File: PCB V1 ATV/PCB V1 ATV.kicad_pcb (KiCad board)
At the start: 2 copper layers, 101.6 x 53.3 mm, 26 parts, among them J1 Power, J10 NW Sensor, J11 N Sensor, J12 NE Sensor, J13 SW Sensor, J14 S Sensor, J15 SE Sensor, J16 Joystick, J17 MotorControl, J2 PWM, J3 Analog, J4 PWM, J5 Analog, J6 Communication, J7 Digital, J8 Battery 12vIN, J9 Motor Controller, SW1 EStop, U1 L7809

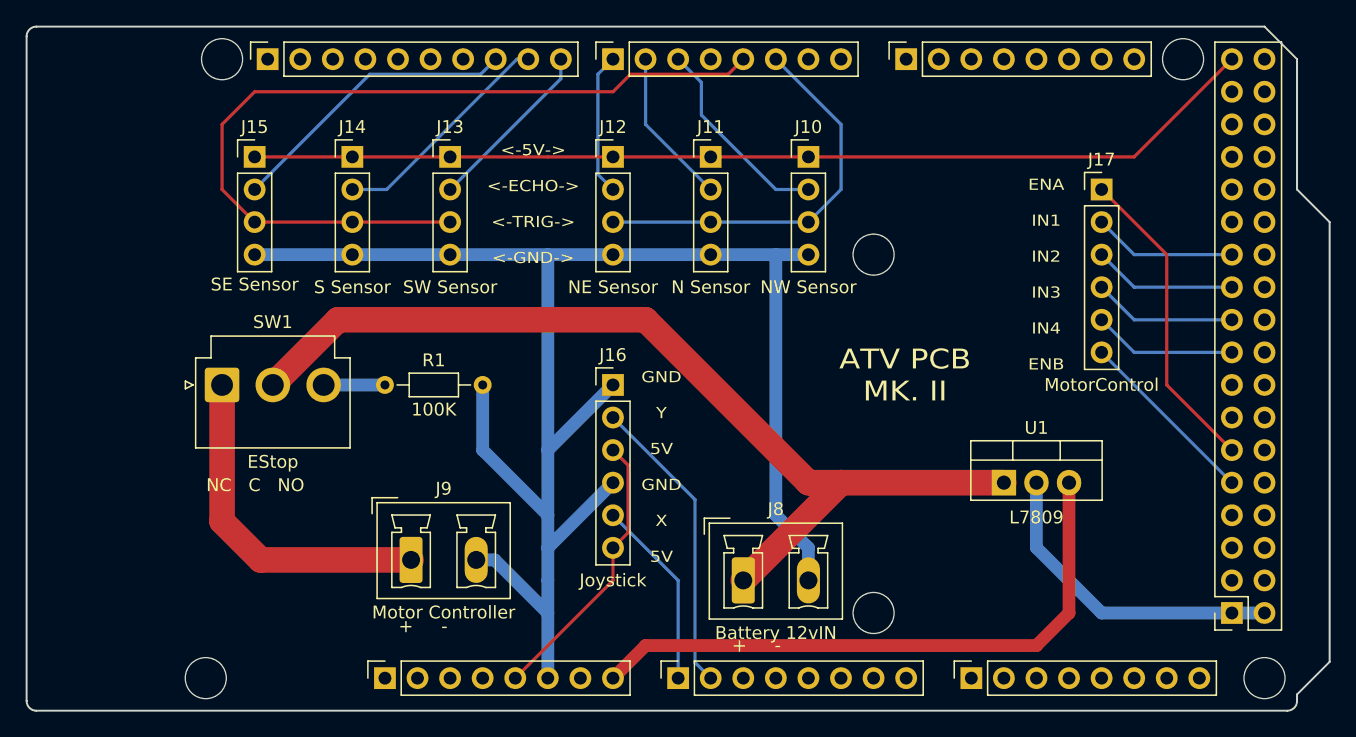
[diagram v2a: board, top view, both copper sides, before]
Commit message: V1.2.1
Updated the silkscreens
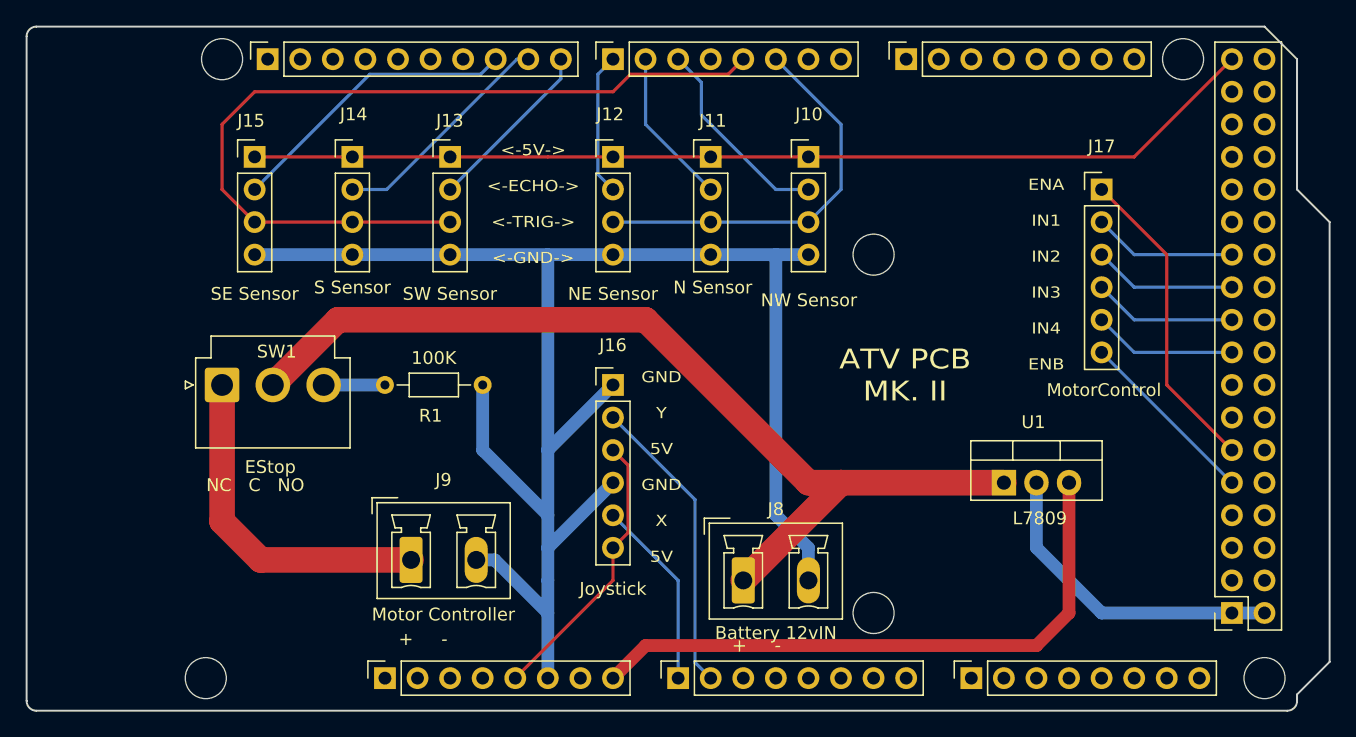
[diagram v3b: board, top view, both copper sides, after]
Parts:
- EStop: renamed from SW1; value EStop -> SW1
- Joystick: renamed from J16; value Joystick -> J16
- L7809: renamed from U1; value L7809 -> U1
- Motor Controller : renamed from J9; value Motor Controller -> J9
- MotorControl: renamed from J17; value MotorControl -> J17
- N Sensor: renamed from J11; value N Sensor -> J11
- NE Sensor: renamed from J12; value NE Sensor -> J12
- NW Sensor: renamed from J10; value NW Sensor -> J10
- S Sensor: renamed from J14; value S Sensor -> J14
- SE Sensor: renamed from J15; value SE Sensor -> J15
- SW Sensor: renamed from J13; value SW Sensor -> J13
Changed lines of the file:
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@@
     (property "ki_keywords" "R res resistor")
     (attr through_hole)
-    (fp_text reference "R1" (at 3.81 -1.92) (layer "F.SilkS")
-        (effects (font (size 1 1) (thickness 0.15)))
-    )
-    (fp_text value "100K" (at 3.81 1.92) (layer "F.SilkS")
+    (fp_text reference "R1" (at 3.56 2.4) (layer "F.SilkS")
+        (effects (font (size 1 1) (thickness 0.15)))
+    )
+    (fp_text value "100K" (at 3.81 -2.1) (layer "F.SilkS")
         (effects (font (size 1 1) (thickness 0.15)))
     )
@@
     (property "ki_keywords" "connector")
     (attr through_hole)
-    (fp_text reference "J9" (at 2.54 -5.55) (layer "F.SilkS")
-        (effects (font (size 1 1) (thickness 0.15)))
-    )
-    (fp_text value "Motor Controller " (at 2.54 4.1) (layer "F.SilkS")
+    (fp_text reference "Motor Controller " (at 2.5225 4.2575) (layer "F.SilkS")
+        (effects (font (size 1 1) (thickness 0.15)))
+    )
+    (fp_text value "J9" (at 2.5225 -6.2425) (layer "F.SilkS")
         (effects (font (size 1 1) (thickness 0.15)))
     )
@@
     (property "ki_keywords" "connector")
     (attr through_hole)
-    (fp_text reference "J17" (at 0 -2.33) (layer "F.SilkS")
-        (effects (font (size 1 1) (thickness 0.15)))
-    )
-    (fp_text value "MotorControl" (at 0 15.24) (layer "F.SilkS")
+    (fp_text reference "MotorControl" (at 0.18 15.64) (layer "F.SilkS")
+        (effects (font (size 1 1) (thickness 0.15)))
+    )
+    (fp_text value "J17" (at 0 -3.36) (layer "F.SilkS")
         (effects (font (size 1 1) (thickness 0.15)))
     )
@@
     (property "ki_keywords" "connector")
     (attr through_hole)
-    (fp_text reference "J15" (at 0 -2.33) (layer "F.SilkS")
-        (effects (font (size 1 1) (thickness 0.15)))
-    )
-    (fp_text value "SE Sensor" (at 0 9.95) (layer "F.SilkS")
+    (fp_text reference "SE Sensor" (at 0 10.68) (layer "F.SilkS")
+        (effects (font (size 1 1) (thickness 0.15)))
+    )
+    (fp_text value "J15" (at -0.28 -2.82) (layer "F.SilkS")
         (effects (font (size 1 1) (thickness 0.15)))
     )
@@
     (property "ki_keywords" "connector")
     (attr through_hole)
-    (fp_text reference "J16" (at 0 -2.33) (layer "F.SilkS")
-        (effects (font (size 1 1) (thickness 0.15)))
-    )
-    (fp_text value "Joystick" (at 0 15.24) (layer "F.SilkS")
+    (fp_text reference "Joystick" (at 0 15.9) (layer "F.SilkS")
+        (effects (font (size 1 1) (thickness 0.15)))
+    )
+    (fp_text value "J16" (at 0 -3.1) (layer "F.SilkS")
         (effects (font (size 1 1) (thickness 0.15)))
     )
@@
     (property "ki_keywords" "connector")
     (attr through_hole)
-    (fp_text reference "J13" (at 0 -2.33) (layer "F.SilkS")
-        (effects (font (size 1 1) (thickness 0.15)))
-    )
-    (fp_text value "SW Sensor" (at 0 10.16) (layer "F.SilkS")
+    (fp_text reference "SW Sensor" (at -0.02 10.68) (layer "F.SilkS")
+        (effects (font (size 1 1) (thickness 0.15)))
+    )
+    (fp_text value "J13" (at -0.02 -2.82) (layer "F.SilkS")
         (effects (font (size 1 1) (thickness 0.15)))
     )
@@
     (property "ki_keywords" "connector")
     (attr through_hole)
-    (fp_text reference "J14" (at 0 -2.33) (layer "F.SilkS")
-        (effects (font (size 1 1) (thickness 0.15)))
-    )
-    (fp_text value "S Sensor" (at 0 10.16) (layer "F.SilkS")
+    (fp_text reference "S Sensor" (at 0 10.18) (layer "F.SilkS")
+        (effects (font (size 1 1) (thickness 0.15)))
+    )
+    (fp_text value "J14" (at 0.1 -3.32) (layer "F.SilkS")
         (effects (font (size 1 1) (thickness 0.15)))
     )
@@
     (property "ki_keywords" "connector")
     (attr through_hole)
-    (fp_text reference "J10" (at 0 -2.33) (layer "F.SilkS")
-        (effects (font (size 1 1) (thickness 0.15)))
-    )
-    (fp_text value "NW Sensor" (at 0 10.16) (layer "F.SilkS")
+    (fp_text reference "NW Sensor" (at 0.04 11.18) (layer "F.SilkS")
+        (effects (font (size 1 1) (thickness 0.15)))
+    )
+    (fp_text value "J10" (at 0.04 -3.32) (layer "F.SilkS")
         (effects (font (size 1 1) (thickness 0.15)))
     )
@@
     (property "ki_keywords" "connector")
     (attr through_hole)
-    (fp_text reference "J11" (at 0 -2.33) (layer "F.SilkS")
-        (effects (font (size 1 1) (thickness 0.15)))
-    )
-    (fp_text value "N Sensor" (at 0 10.16) (layer "F.SilkS")
+    (fp_text reference "N Sensor" (at 0.16 10.18) (layer "F.SilkS")
+        (effects (font (size 1 1) (thickness 0.15)))
+    )
+    (fp_text value "J11" (at 0.16 -2.82) (layer "F.SilkS")
         (effects (font (size 1 1) (thickness 0.15)))
     )
@@
     (property "ki_keywords" "Voltage Regulator 1.5A Positive")
     (attr through_hole)
-    (fp_text reference "U1" (at 2.54 -4.27) (layer "F.SilkS")
-        (effects (font (size 1 1) (thickness 0.15)))
-    )
-    (fp_text value "L7809" (at 2.54 2.71) (layer "F.SilkS")
+    (fp_text reference "L7809" (at 2.8 2.78) (layer "F.SilkS")
+        (effects (font (size 1 1) (thickness 0.15)))
+    )
+    (fp_text value "U1" (at 2.3 -4.72) (layer "F.SilkS")
         (effects (font (size 1 1) (thickness 0.15)))
     )
@@
     (property "ki_keywords" "switch dual-pole double-throw DPDT spdt ON-ON")
     (attr through_hole)
-    (fp_text reference "SW1" (at 3.96 -4.9) (layer "F.SilkS")
-        (effects (font (size 1 1) (thickness 0.15)))
-    )
-    (fp_text value "EStop" (at 3.96 6) (layer "F.SilkS")
+    (fp_text reference "EStop" (at 3.76 6.4) (layer "F.SilkS")
+        (effects (font (size 1 1) (thickness 0.15)))
+    )
+    (fp_text value "SW1" (at 4.26 -2.6) (layer "F.SilkS")
         (effects (font (size 1 1) (thickness 0.15)))
     )
@@
     (property "ki_keywords" "connector")
     (attr through_hole)
-    (fp_text reference "J12" (at 0 -2.33) (layer "F.SilkS")
-        (effects (font (size 1 1) (thickness 0.15)))
-    )
-    (fp_text value "NE Sensor" (at 0 10.16) (layer "F.SilkS")
+    (fp_text reference "NE Sensor" (at 0 10.68) (layer "F.SilkS")
+        (effects (font (size 1 1) (thickness 0.15)))
+    )
+    (fp_text value "J12" (at -0.22 -3.32) (layer "F.SilkS")
         (effects (font (size 1 1) (thickness 0.15)))
     )
@@
     (effects (font (size 0.87 1) (thickness 0.15)) (justify bottom))
   )
-  (gr_text "+     -\n" (at 129 94) (layer "F.SilkS")
+  (gr_text "+     -\n" (at 129 95) (layer "F.SilkS")
     (effects (font (size 1 1) (thickness 0.15)) (justify left bottom))
   )
